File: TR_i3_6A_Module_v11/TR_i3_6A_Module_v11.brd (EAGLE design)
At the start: 62 x 44 mm, 35 parts, among them CN1 VL-2P, CN2 VL-3P, CN3 XA-2P, CN4 EH-2P, IC1 I3A, IC2 I6A, IC3 TLP172G, Q1 BSS138

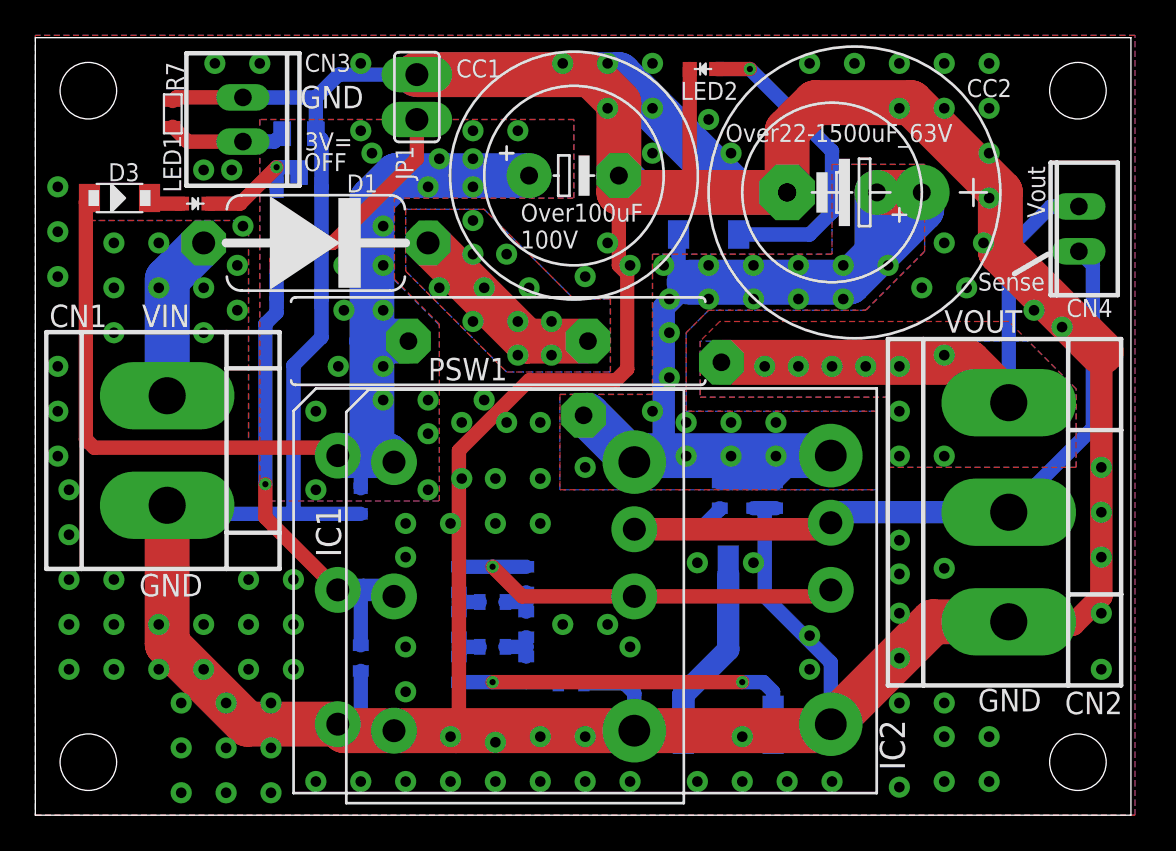
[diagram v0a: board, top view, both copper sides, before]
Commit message: TR製DCDCモジュール（ストロベリーリナックスのLT3790モジュールの代替品）
レイアウト修正
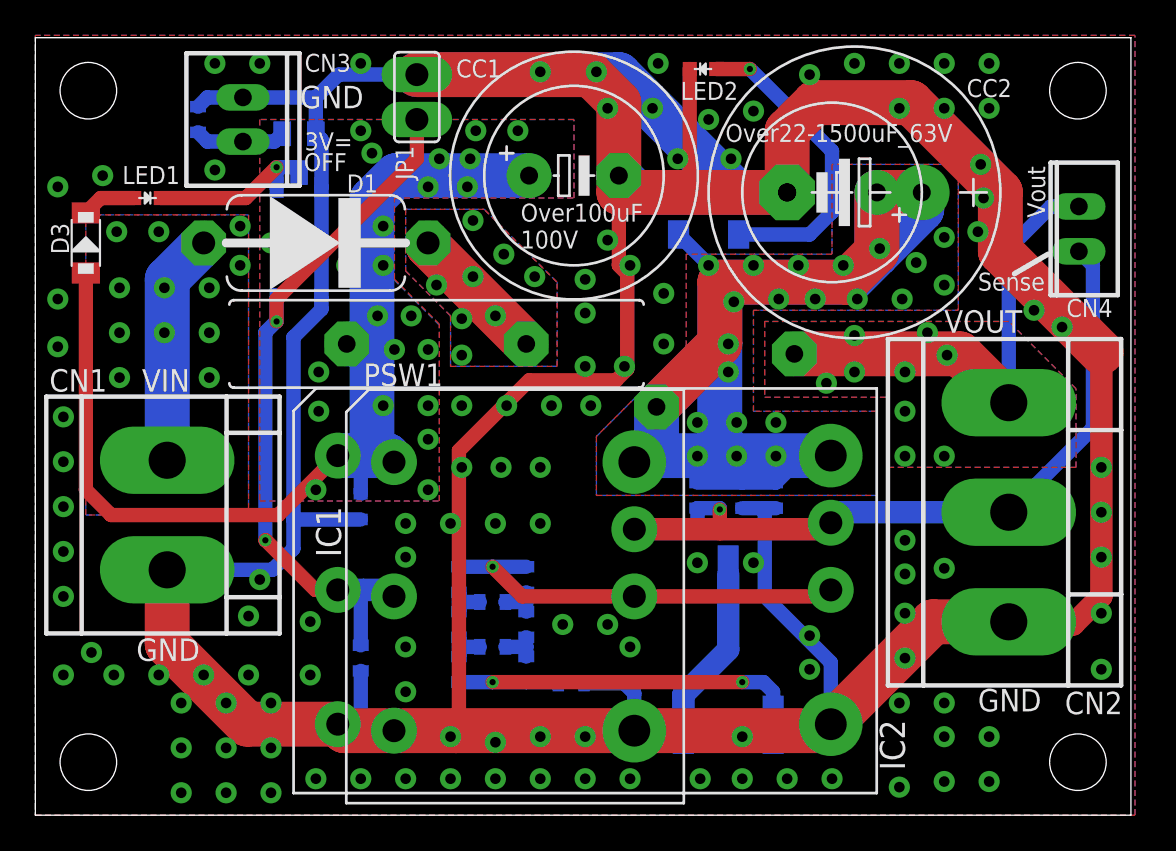
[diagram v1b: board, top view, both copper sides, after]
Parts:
- moved NTC1 4.15 mm to (39.1, 24.6)
- moved CN1 3.65 mm to (7.46, 17.0)
- moved PSW1 3.50 mm to (22.7, 26.7)
- moved D3 3.17 mm to (2.86, 32.4), turned to 270 degrees
- moved LED1 2.72 mm to (6.35, 34.9)
- moved R7 1.46 mm to (9.21, 39.4), flipped to the bottom
- moved JP3 1.27 mm to (37.5, 18.1)
- moved C2 0.63 mm to (40.0, 18.1)
- moved C1 0.32 mm to (18.4, 17.5)
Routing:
- net OUT+: track 59.9 -> 84.3 mm
- net VOUT: track 30.9 -> 27.0 mm
- net VIN: track 9.50 -> 13.2 mm, vias 10 -> 12
- net D_PSW: track 11.4 -> 8.02 mm, vias 11 -> 8
- net N$10: track 7.24 -> 9.81 mm
- net GND: track 318.2 -> 316.1 mm, vias 120 -> 117
- net N$4: track 39.7 -> 41.7 mm
- net SENSE: track 44.0 -> 45.9 mm, vias 0 -> 1
- net !ENABLE: track 6.73 -> 5.17 mm
- net N$6: track 1.97 -> 3.09 mm
- net IN+: track 59.8 -> 59.6 mm, vias 21 -> 24

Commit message: TR製DCDCモジュール（ストロベリーリナックスのLT3790モジュールの代替品）
レイアウト・ビア修正
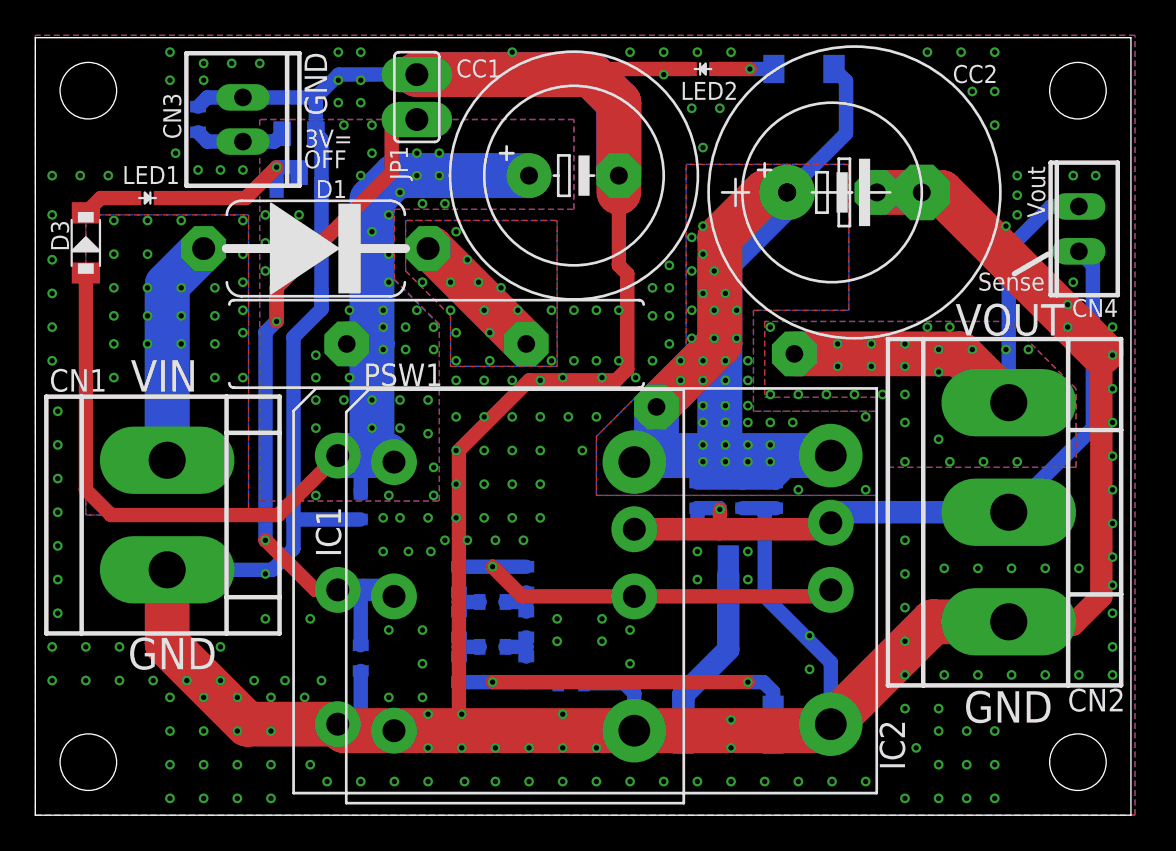
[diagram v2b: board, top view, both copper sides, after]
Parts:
- moved D2 10.8 mm to (43.5, 42.2), turned to 180 degrees
- moved D1 0.32 mm to (15.9, 32.1)
- turned CC2 to 0 degrees
- turned CC2\ to 0 degrees
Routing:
- net GND: track 316.1 -> 259.7 mm, vias 117 -> 223
- net N$5: track 17.7 -> 3.27 mm
- net OUT+: track 84.3 -> 74.1 mm, vias 21 -> 40
- net N$4: track 41.7 -> 42.6 mm
- net VIN: track 13.2 -> 12.8 mm, vias 12 -> 25
- net D_PSW: track 8.02 -> 7.79 mm, vias 8 -> 15
- net VOUT: vias 9 -> 26
- net IN+: vias 24 -> 46
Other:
- board text added: "100V"
- board text added: "Over 100uF"
- board text added: "Over22- 1500uF_63V"
- board text added: "Short =ON"
- board text removed: "Over100uF 100V"
- board text removed: "Over22-1500uF_63V"

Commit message: TR製DCDCモジュール（ストロベリーリナックスのLT3790モジュールの代替品）
基板データ更新
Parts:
- moved NTC1 0.48 mm to (39.1, 24.1)
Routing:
- net OUT+: track 74.1 -> 74.2 mm, vias 40 -> 41
- net VIN: vias 25 -> 31
- net IN+: vias 46 -> 50
- net GND: vias 223 -> 235

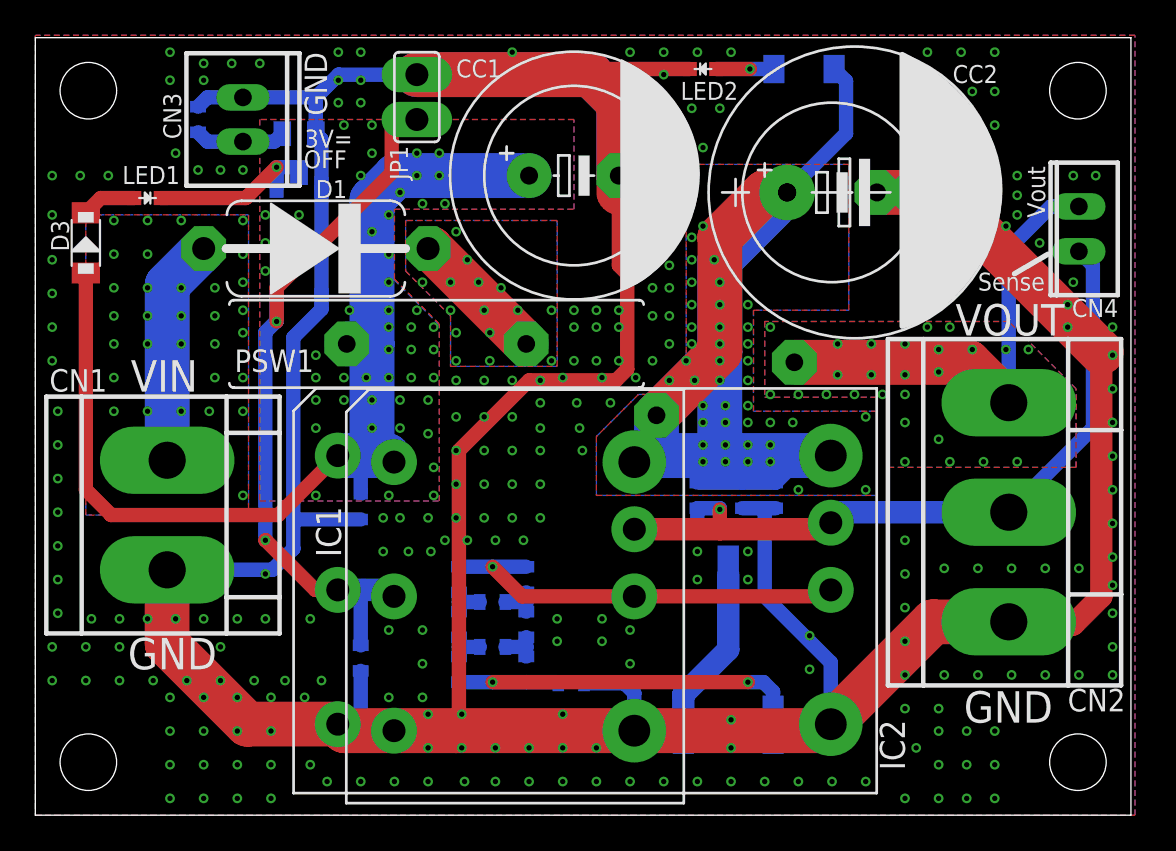
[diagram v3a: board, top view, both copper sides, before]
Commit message: TR製DCDCモジュール（ストロベリーリナックスのLT3790モジュールの代替品）
レジスト開口部の修正。（指摘画像あり）
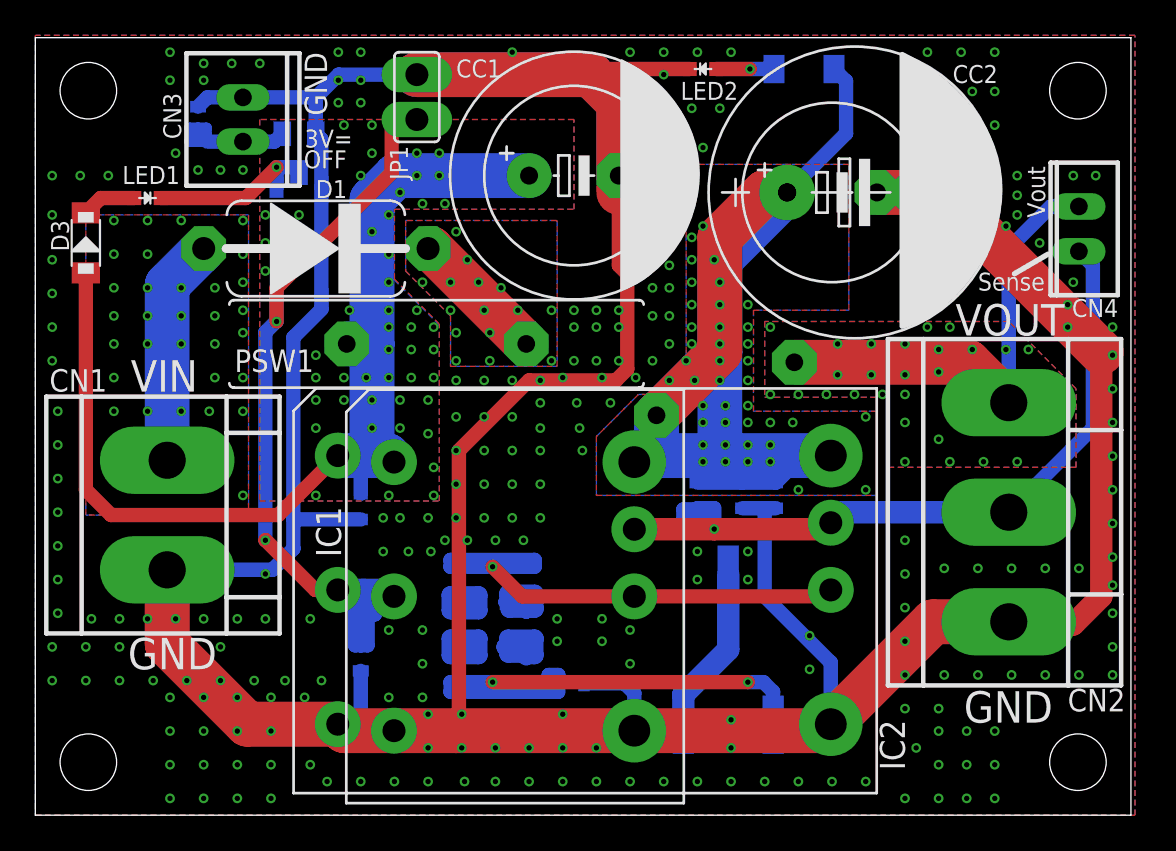
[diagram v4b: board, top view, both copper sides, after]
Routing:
- net N$1: track 23.6 -> 32.6 mm
- net N$4: track 42.6 -> 49.4 mm
- net N$7: track 23.8 -> 30.3 mm
- net N$9: track 2.27 -> 7.41 mm
- net N$8: track 2.27 -> 7.30 mm
- net N$3: track 2.27 -> 7.28 mm
- net N$2: track 2.27 -> 7.21 mm
- net SENSE: track 45.9 -> 49.9 mm
- net !ENABLE: track 5.17 -> 8.35 mm
